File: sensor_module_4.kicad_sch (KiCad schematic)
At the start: 42 parts, among them J18 EZO Carrier Board, J6 Cal_in, U15 TLV4387, U4 TLV2387DGKR

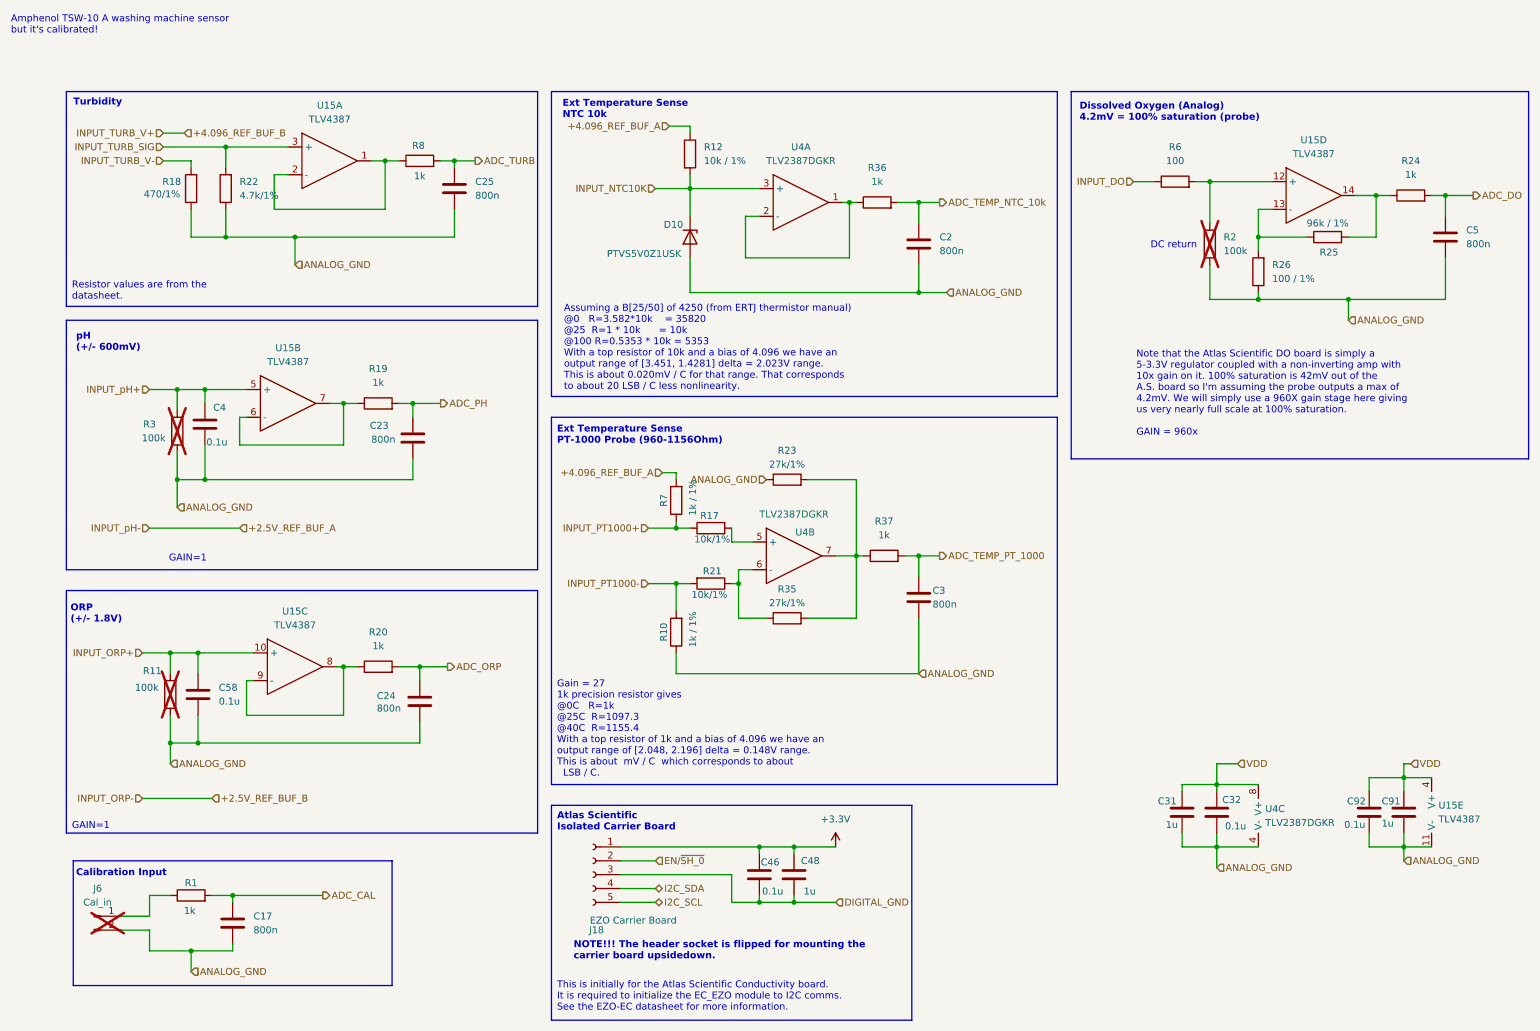
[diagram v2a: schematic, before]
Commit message: BUG FIX -------- There were some issues with the board WRT manufacturing. I changed the VSSOP 8 packages to SOT versions and re-routed
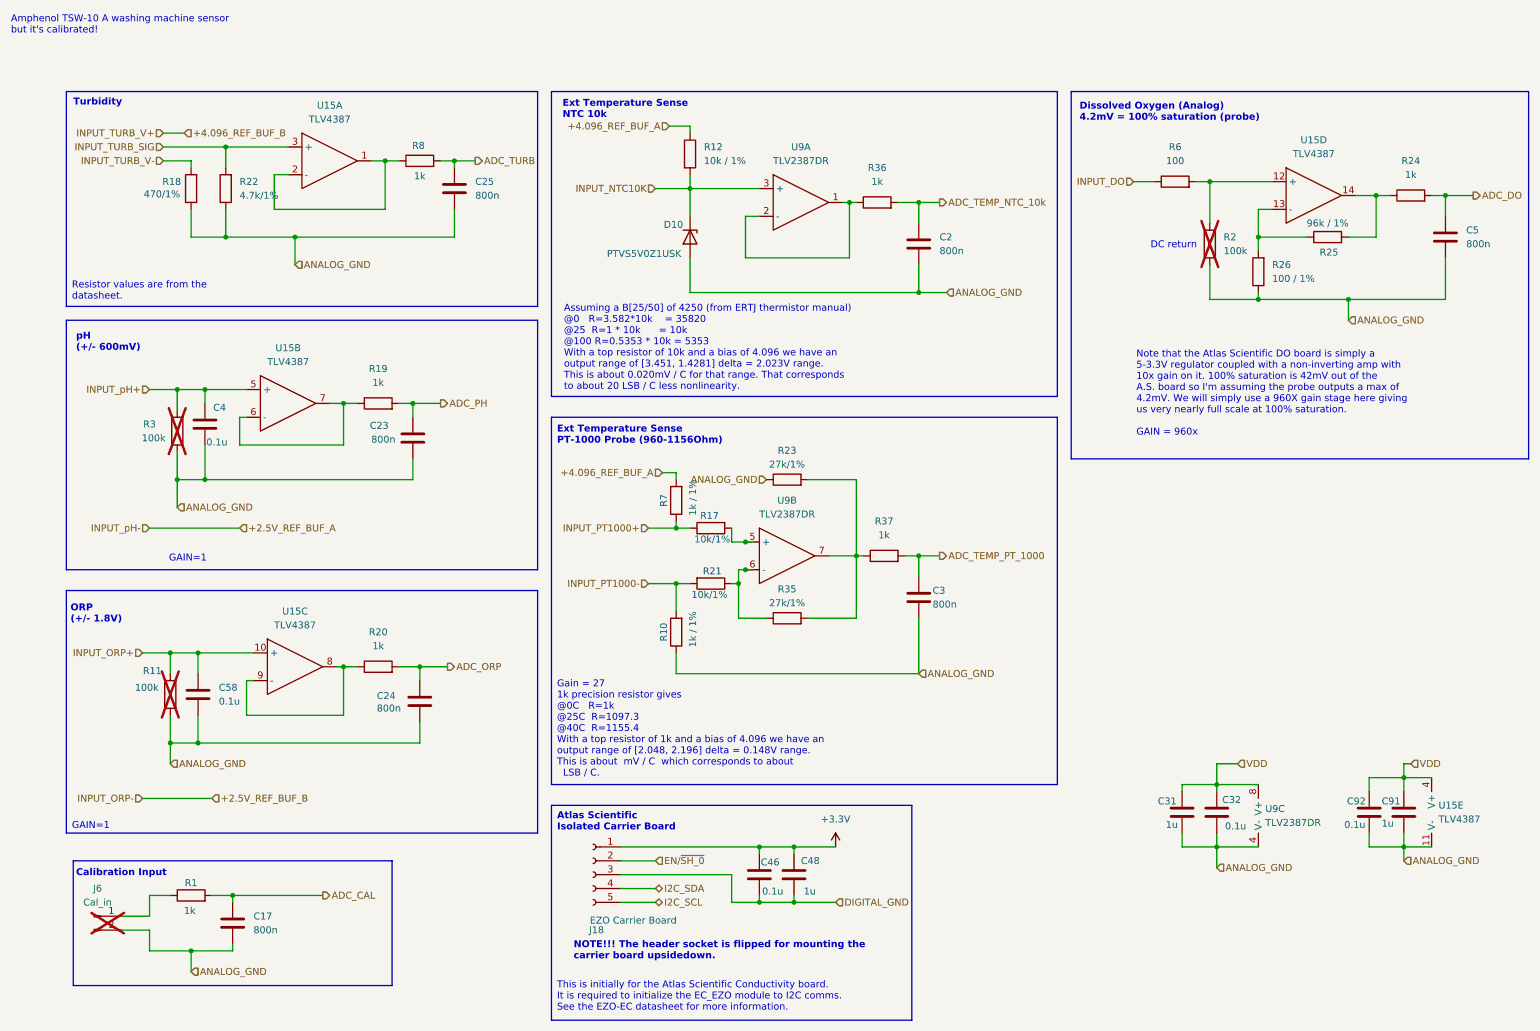
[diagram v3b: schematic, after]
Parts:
- removed U4: TLV2387DGKR, Package_SO:VSSOP-8_3x3mm_P0.65mm, symbol Op-Amp-Extended:TLV2387DGKR
- added U9: TLV2387DR, Package_SO:SOIC-8_3.9x4.9mm_P1.27mm, symbol Op-Amp-Extended:TLV2387DR
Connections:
- net ANALOG_GND: now also U9.4 (V-)
- net INPUT_NTC10K: now also U9.3 (+)
- net VDD: now also U9.8 (V+)
- net at R17.2: now also U9.5 (+)
- net at R21.1, R35.1: now also U9.6 (-)
- net at R36.1: now also U9.1, U9.2 (-)
- net at R23.2, R35.2, R37.1: now also U9.7

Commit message: Maintenance update - Adding the EC isolation board schematic - Added a harness page for wireing module together
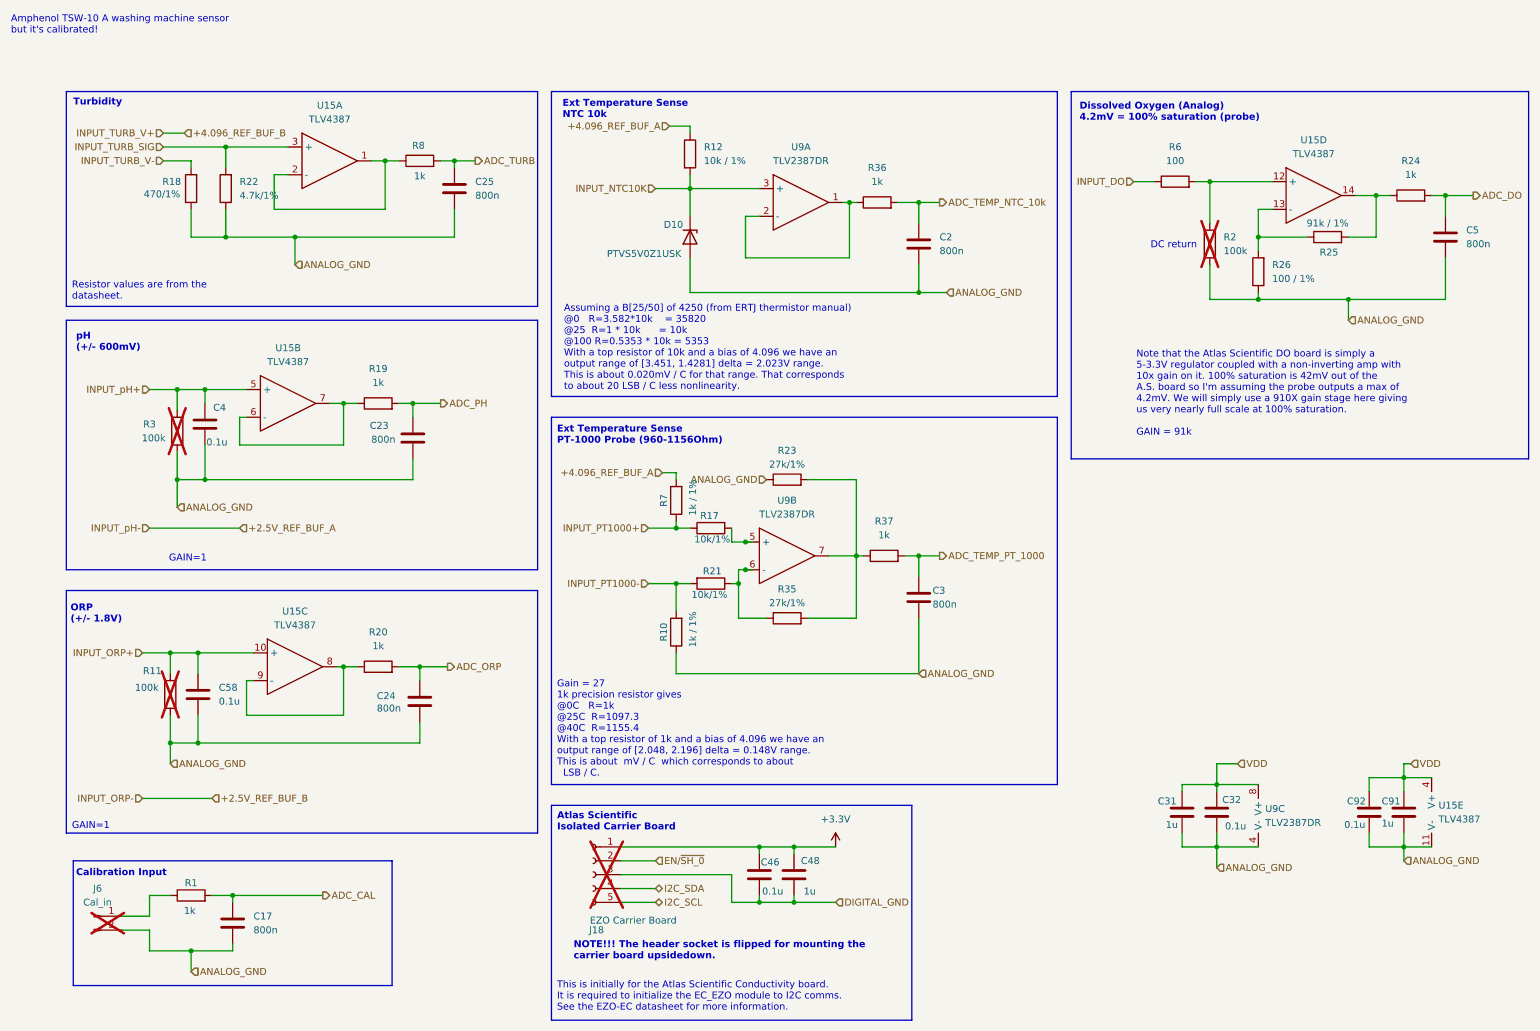
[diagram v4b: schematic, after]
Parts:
- C17, C2, C23, C24, C25, C3, C5: MPN (none) -> CC0805KKX7R7BB824; Manufacturer (none) -> YAGEO; Package (none) -> 0805
- C31, C48, C91: MPN (none) -> CL21B105KOFNNNG; Manufacturer (none) -> Samsung; Package (none) -> 0805
- C32, C4, C46, C58, C92: MPN (none) -> CC0805KRX7R7BB104; Manufacturer (none) -> YAGEO; Package (none) -> 0805
- D10: MPN (none) -> PTVS5V0Z1USK; Manufacturer (none) -> Nexperia; Package (none) -> DSN1608-2
- J18: now not fitted
- R1, R10, R19, R20, R24, R36, R37, R7, R8: MPN (none) -> AC0805FR-7W1KL; Manufacturer (none) -> YAGEO; Package (none) -> 0805
- R11, R2, R3: MPN (none) -> AC0805FR-7W100KL; Manufacturer (none) -> YAGEO; Package (none) -> 0805
- R12, R17, R21: MPN (none) -> AC0805FR-7W10KL; Manufacturer (none) -> YAGEO; Package (none) -> 0805
- R18: MPN (none) -> RCC0805470RFKEA; Manufacturer (none) -> Vishay-Dale; Package (none) -> 0805
- R22: MPN (none) -> AC0805FR-7W4K7L; Manufacturer (none) -> YAGEO; Package (none) -> 0805
- R23, R35: MPN (none) -> RC0805FR-7W27KL; Manufacturer (none) -> YAGEO; Package (none) -> 0805
- R25: value 96k / 1% -> 91k / 1%; MPN (none) -> AC0805FR-7W91KL; Manufacturer (none) -> YAGEO; Package (none) -> 0805
- R26, R6: MPN (none) -> AC0805FR-7W100RL; Manufacturer (none) -> YAGEO; Package (none) -> 0805
- U15: MPN (none) -> TLV4387PWR; Manufacturer (none) -> TI; Package (none) -> TSSOP-14
- U9: MPN (none) -> TLV2387DR; Manufacturer (none) -> TI; Package (none) -> SOIC-8
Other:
- note added: "Note that the Atlas Scientific DO board is simply a 5-3.3V regulator coupled with a non-inverting amp with 10x gain on it. 100% saturation is 42mV out of the A.S. board so I'm assuming the probe outputs a max of 4.2mV. We will simply use a 910X gain stage here giving us very nearly full scale at 100% saturation. GAIN = 91k"
- note removed: "Note that the Atlas Scientific DO board is simply a 5-3.3V regulator coupled with a non-inverting amp with 10x gain on it. 100% saturation is 42mV out of the A.S. board so I'm assuming the probe outputs a max of 4.2mV. We will simply use a 960X gain stage here giving us very nearly full scale at 100% saturation. GAIN = 960x"
